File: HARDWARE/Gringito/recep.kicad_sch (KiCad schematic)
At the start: 28 parts, among them J3 Conn_01x02, U6 BQ51013BRHLR, U7 MCP73831T-2ATI/OT, U8 PTPS7A2033PDBVR

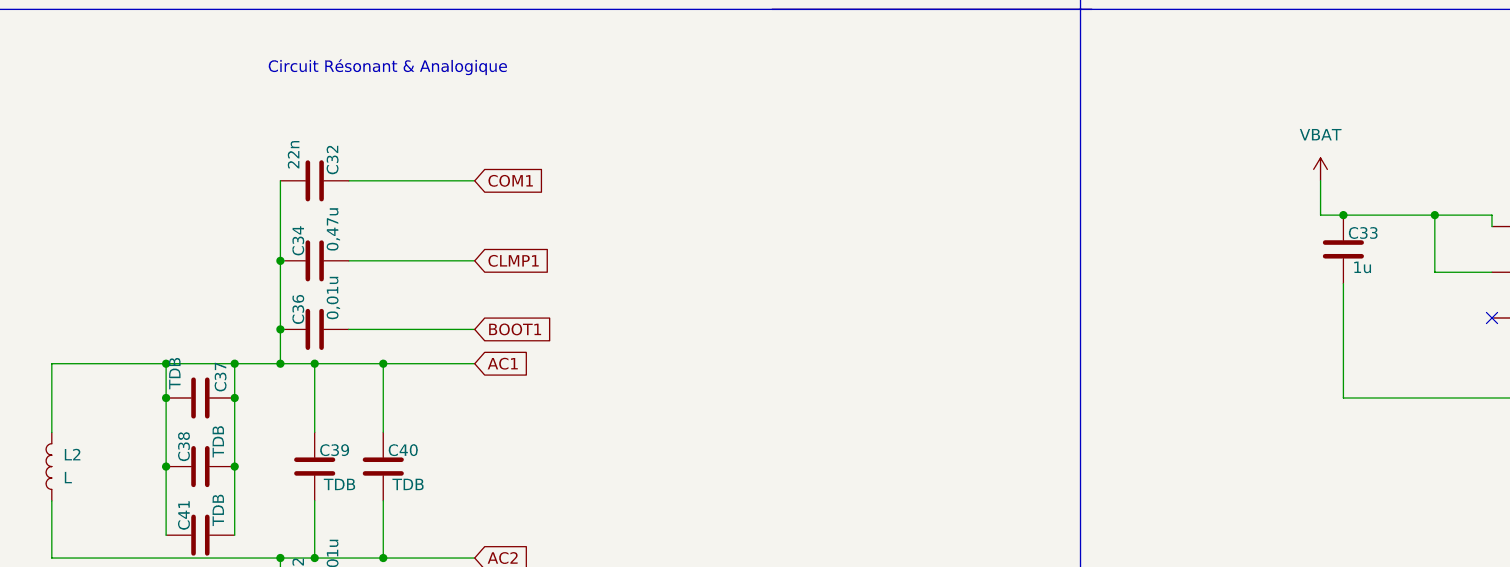
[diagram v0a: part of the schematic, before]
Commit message: V1 PCB Wireless charging
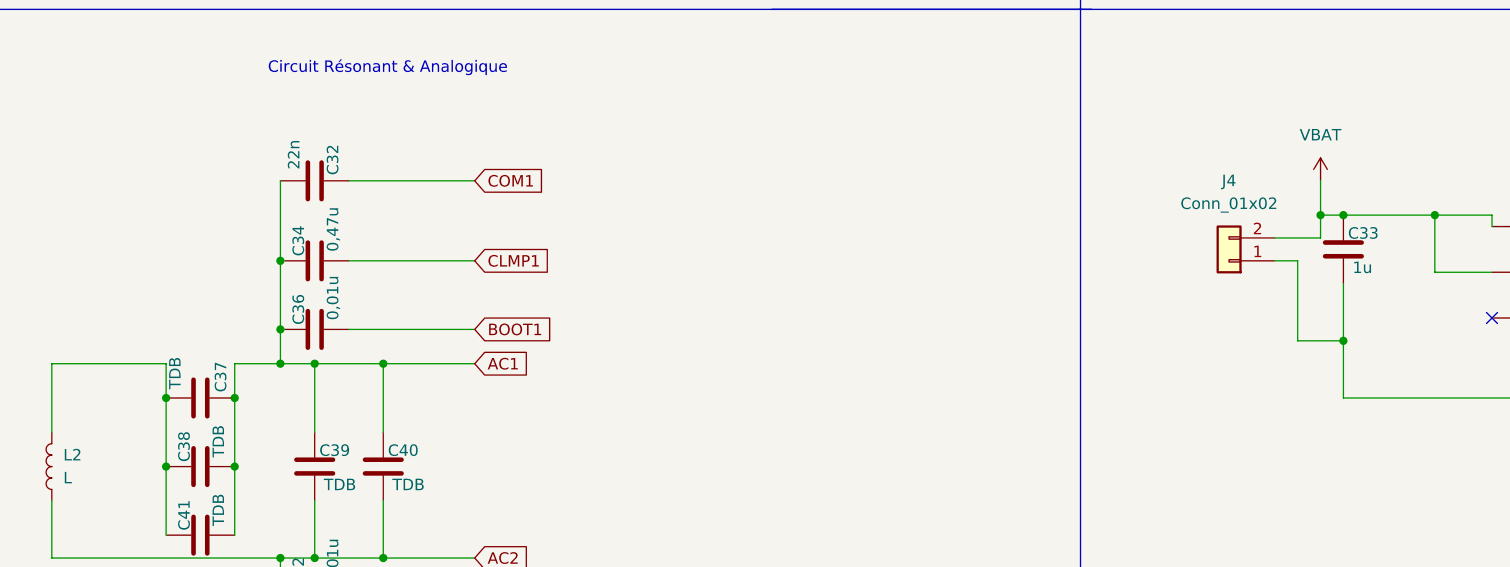
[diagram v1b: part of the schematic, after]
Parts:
- added J4: Conn_01x02, Connector_PinHeader_2.54mm:PinHeader_1x02_P2.54mm_Vertical, symbol Connector_Generic:Conn_01x02
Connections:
- net AC1: no longer C37.2, C38.1, C41.1, L2.2
- net GND1: now also J4.1 (Pin_1)
- net VBAT: now also J4.2 (Pin_2)
- new net: C37.2, C38.1, C41.1, L2.2
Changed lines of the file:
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@@
 	)
 	(junction
-		(at 80.01 139.7)
+		(at 194.31 137.16)
 		(diameter 0)
 		(color 0 0 0 0)
 	)
 	(junction
-		(at 76.2 161.29)
+		(at 80.01 139.7)
 		(diameter 0)
 		(color 0 0 0 0)
 	)
 	(junction
-		(at 194.31 123.19)
+		(at 76.2 161.29)
 		(diameter 0)
 		(color 0 0 0 0)
 	)
 	(junction
-		(at 63.5 139.7)
+		(at 194.31 123.19)
 		(diameter 0)
 		(color 0 0 0 0)
@@
 	)
 	(junction
-		(at 71.12 139.7)
-		(diameter 0)
-		(color 0 0 0 0)
-	)
-	(junction
 		(at 127 80.01)
 		(diameter 0)
@@
 	)
 	(junction
+		(at 191.77 123.19)
+		(diameter 0)
+		(color 0 0 0 0)
+	)
+	(junction
 		(at 76.2 172.72)
 		(diameter 0)
@@
 	(wire
 		(pts
+			(xy 186.69 128.27) (xy 189.23 128.27)
+		)
+		(stroke
+			(width 0)
+			(type default)
+		)
+	)
+	(wire
+		(pts
 			(xy 210.82 123.19) (xy 210.82 124.46)
 		)
@@
 	(wire
 		(pts
-			(xy 71.12 139.7) (xy 63.5 139.7)
+			(xy 194.31 137.16) (xy 194.31 143.51)
 		)
 		(stroke
@@
 	(wire
 		(pts
-			(xy 194.31 130.81) (xy 194.31 143.51)
+			(xy 194.31 130.81) (xy 194.31 137.16)
 		)
 		(stroke
@@
 	(wire
 		(pts
+			(xy 189.23 137.16) (xy 194.31 137.16)
+		)
+		(stroke
+			(width 0)
+			(type default)
+		)
+	)
+	(wire
+		(pts
 			(xy 134.62 34.29) (xy 138.43 34.29)
 		)
@@
 	(wire
 		(pts
+			(xy 186.69 125.73) (xy 191.77 125.73)
+		)
+		(stroke
+			(width 0)
+			(type default)
+		)
+	)
+	(wire
+		(pts
 			(xy 242.57 52.07) (xy 261.62 52.07)
 		)
@@
 	(wire
 		(pts
+			(xy 191.77 125.73) (xy 191.77 123.19)
+		)
+		(stroke
+			(width 0)
+			(type default)
+		)
+	)
+	(wire
+		(pts
 			(xy 49.53 57.15) (xy 53.34 57.15)
 		)
@@
 		)
 	)
+	(wire
+		(pts
+			(xy 189.23 128.27) (xy 189.23 137.16)
+		)
+		(stroke
+			(width 0)
+			(type default)
+		)
+	)
 	(global_label "AC2"
 		(shape input)
@@
 					(unit 1)
 				)
+			)
+		)
+	)
+	(symbol
+		(lib_id "Connector_Generic:Conn_01x02")
+		(at 181.61 128.27 180)
+		(unit 1)
+		(exclude_from_sim no)
+		(in_bom yes)
+		(on_board yes)
+		(dnp no)
+		(fields_autoplaced yes)
+		(property "Reference" "J4"
+			(at 181.61 119.38 0)
+			(effects
+				(font
+					(size 1.27 1.27)
+				)
+			)
+		)
+		(property "Value" "Conn_01x02"
+			(at 181.61 121.92 0)
+			(effects
+				(font
+					(size 1.27 1.27)
+				)
+			)
+		)
+		(property "Footprint" "Connector_PinHeader_2.54mm:PinHeader_1x02_P2.54mm_Vertical"
+			(at 181.61 128.27 0)
+			(effects
+				(font
+					(size 1.27 1.27)
+				)
+				(hide yes)
+			)
+		)
+		(property "Datasheet" "~"
+			(at 181.61 128.27 0)
+			(effects
+				(font
+					(size 1.27 1.27)
+				)
+				(hide yes)
+			)
+		)
+		(property "Description" "Generic connector, single row, 01x02, script generated (kicad-library-utils/schlib/autogen/connector/)"
+			(at 181.61 128.27 0)
+			(effects
+				(font
+					(size 1.27 1.27)
+				)
+				(hide yes)
+			)
+		)
+		(pin "2"
+		)
+		(pin "1"
+		)
+		(instances
+			(project "Gringito"
+				(path "/b72a56c5-f9ec-4576-b7ce-b467e19fda9b/470eb5a5-9a20-43a6-b8ca-581ac88d1304"
+					(reference "J4")
+					(unit 1)
+				)
